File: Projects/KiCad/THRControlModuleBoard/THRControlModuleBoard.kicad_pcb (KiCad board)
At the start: 2 copper layers, 153.6 x 96.2 mm, 36 parts, among them IC1 LTC1480CN8#PBF, IC2 LTC1480CN8#PBF, J1 Conn_01x02_Socket, J2 Conn_01x02_Socket, J3 Screw_Terminal_01x02, J4 Conn_01x04_Socket, J5 Conn_01x04_Socket, J6 PCC-SMP-K-5, Q1 Q_PMOS_GDS, Q2 Q_PMOS_GDS, Q3 Q_PMOS_GDS, U1 LTC4416EMS#PBF, U2 MAX31856MUD+T, U3 NUCLEO-F303K8

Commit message: THRControlModuleを更新
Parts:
- moved IC1 45.0 mm to (181.8, 107.4)
- moved J4 45.0 mm to (182.1, 118.2)
- moved J3 42.3 mm to (180.5, 76.3)
- moved D1 37.1 mm to (168.7, 98.3)
- moved D2 37.1 mm to (165.6, 98.3)
- moved D3 37.1 mm to (171.7, 98.3)
- moved R7 37.1 mm to (165.6, 91.4)
- moved R8 37.1 mm to (171.7, 91.4)
- moved C3 37.1 mm to (152.9, 94.2)
- moved C4 37.1 mm to (152.9, 97.8)
- moved C6 37.1 mm to (152.9, 90.6)
- moved J6 37.1 mm to (159.1, 72.5)
- moved R6 37.1 mm to (168.7, 91.4)
- moved U2 37.1 mm to (158.5, 93.4)
- moved C5 37.1 mm to (158.8, 87.3)
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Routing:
- net RS485__ENABLE: track 0.00 -> 5.08 mm
- added copper zone on F.Cu, net Main Power Supply
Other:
- board size 153.6 x 96.2 mm -> 88.4 x 65.6 mm

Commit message: さーぼうごかしたい
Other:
- board size 88.4 x 65.6 mm -> 110 x 95.2 mm
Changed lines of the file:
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@@
   )
   (setup
+    (stackup
+      (layer "F.SilkS" (type "Top Silk Screen"))
+      (layer "F.Paste" (type "Top Solder Paste"))
+      (layer "F.Mask" (type "Top Solder Mask") (thickness 0.01))
+      (layer "F.Cu" (type "copper") (thickness 0.035))
+      (layer "dielectric 1" (type "core") (thickness 1.51) (material "FR4") (epsilon_r 4.5) (loss_tangent 0.02))
+      (layer "B.Cu" (type "copper") (thickness 0.035))
+      (layer "B.Mask" (type "Bottom Solder Mask") (thickness 0.01))
+      (layer "B.Paste" (type "Bottom Solder Paste"))
+      (layer "B.SilkS" (type "Bottom Silk Screen"))
+      (copper_finish "None")
+      (dielectric_constraints no)
+    )
     (pad_to_mask_clearance 0)
     (pcbplotparams
@@
     )
   )
-  (gr_line (start 187.7 126) (end 109.9 126)
-    (stroke (width 0.1) (type default)) (layer "Edge.Cuts"))
-  (gr_line (start 191.01 60.431) (end 102.61 60.431)
-    (stroke (width 0.1) (type default)) (layer "Edge.Cuts"))
+  (gr_circle (center 145.4 96.6) (end 145.5 96.6)
+    (stroke (width 0.0001) (type solid)) (fill solid) (layer "Edge.Cuts"))
+  (gr_circle (center 145.4 96.6) (end 145.5 96.6)
+    (stroke (width 0.0001) (type solid)) (fill solid) (layer "Edge.Cuts"))
+  (gr_arc (start 107.890168 136.6) (mid 145.4 41.375474) (end 182.909832 136.6)
+    (stroke (width 0.2) (type solid)) (layer "Edge.Cuts"))
+  (gr_circle (center 145.4 96.6) (end 145.5 96.6)
+    (stroke (width 0.0001) (type solid)) (fill solid) (layer "Edge.Cuts"))
+  (gr_circle (center 145.4 96.6) (end 145.5 96.6)
+    (stroke (width 0.0001) (type solid)) (fill solid) (layer "Edge.Cuts"))
+  (gr_circle (center 145.4 96.6) (end 145.5 96.6)
+    (stroke (width 0.0001) (type solid)) (fill solid) (layer "Edge.Cuts"))
+  (gr_circle (center 145.4 96.6) (end 145.5 96.6)
+    (stroke (width 0.0001) (type solid)) (fill solid) (layer "Edge.Cuts"))
+  (gr_circle (center 145.4 96.6) (end 145.5 96.6)
+    (stroke (width 0.0001) (type solid)) (fill solid) (layer "Edge.Cuts"))
+  (gr_circle (center 145.4 96.6) (end 145.5 96.6)
+    (stroke (width 0.0001) (type solid)) (fill solid) (layer "Edge.Cuts"))
+  (gr_circle (center 145.4 96.6) (end 145.5 96.6)
+    (stroke (width 0.0001) (type solid)) (fill solid) (layer "Edge.Cuts"))
+  (gr_circle (center 145.4 96.6) (end 145.5 96.6)
+    (stroke (width 0.0001) (type solid)) (fill solid) (layer "Edge.Cuts"))
+  (gr_circle (center 145.4 96.6) (end 145.5 96.6)
+    (stroke (width 0.0001) (type solid)) (fill solid) (layer "Edge.Cuts"))
+  (gr_circle (center 145.4 96.6) (end 145.5 96.6)
+    (stroke (width 0.0001) (type solid)) (fill solid) (layer "Edge.Cuts"))
+  (gr_line (start 182.909832 136.6) (end 107.890168 136.6)
+    (stroke (width 0.2) (type solid)) (layer "Edge.Cuts"))
+  (gr_circle (center 145.4 96.6) (end 145.5 96.6)
+    (stroke (width 0.0001) (type solid)) (fill solid) (layer "Edge.Cuts"))
+  (gr_circle (center 145.4 96.6) (end 145.5 96.6)
+    (stroke (width 0.0001) (type solid)) (fill solid) (layer "Edge.Cuts"))
+  (gr_circle (center 145.4 96.6) (end 145.5 96.6)
+    (stroke (width 0.0001) (type solid)) (fill solid) (layer "Edge.Cuts"))
   (segment (start 114.51 68.7485) (end 114.51 70.7535) (width 1) (layer "F.Cu") (net 1))
   (segment (start 123.912 77.184) (end 123.912 80.4215) (width 0.25) (layer "F.Cu") (net 1))
@@
     )
   )
+  (group "" (id 6e8ac5b0-bd87-4622-b2de-0a6718457d24)
+    (members
+      02eda940-add0-4b54-9729-b477d0ac1bd8
+      0f6cd9d3-a6ce-4f51-8e13-86931dcd8bd2
+      16407f10-dc8b-4954-87af-a99fab043be2
+      1663ffb2-55dc-4813-a6c3-30438c59a478
+      2d43c464-5b90-429b-b19e-6585a19991ff
+      2ef0aaf6-961e-416b-b369-ce24fa3bbbf0
+      54b76117-5f5b-4763-8b0f-193e03239677
+      6ae3d9e0-deb5-44b5-9874-15ed370a52bc
+      7051c1c9-aa6a-4af1-a04f-d4374640d7f7
+      7994f68a-6575-4db6-a7d5-2af3b2de868c
+      9ebd4081-3d82-469b-948d-cb647f83ce62
+      adc2bde1-7d6a-4060-a991-f76b2fa04667
+      da316a41-3531-4383-ad27-9925a38623bb
+      de768a8c-8413-48a7-8f38-190f8ccf8624
+      dec51251-748c-4501-a1a5-cca1334c7dda
+      dfc7496d-4f87-4a89-9541-c43c7443b227
+      e50dee0a-0c97-447f-b977-912c927439fb
+    )
+  )

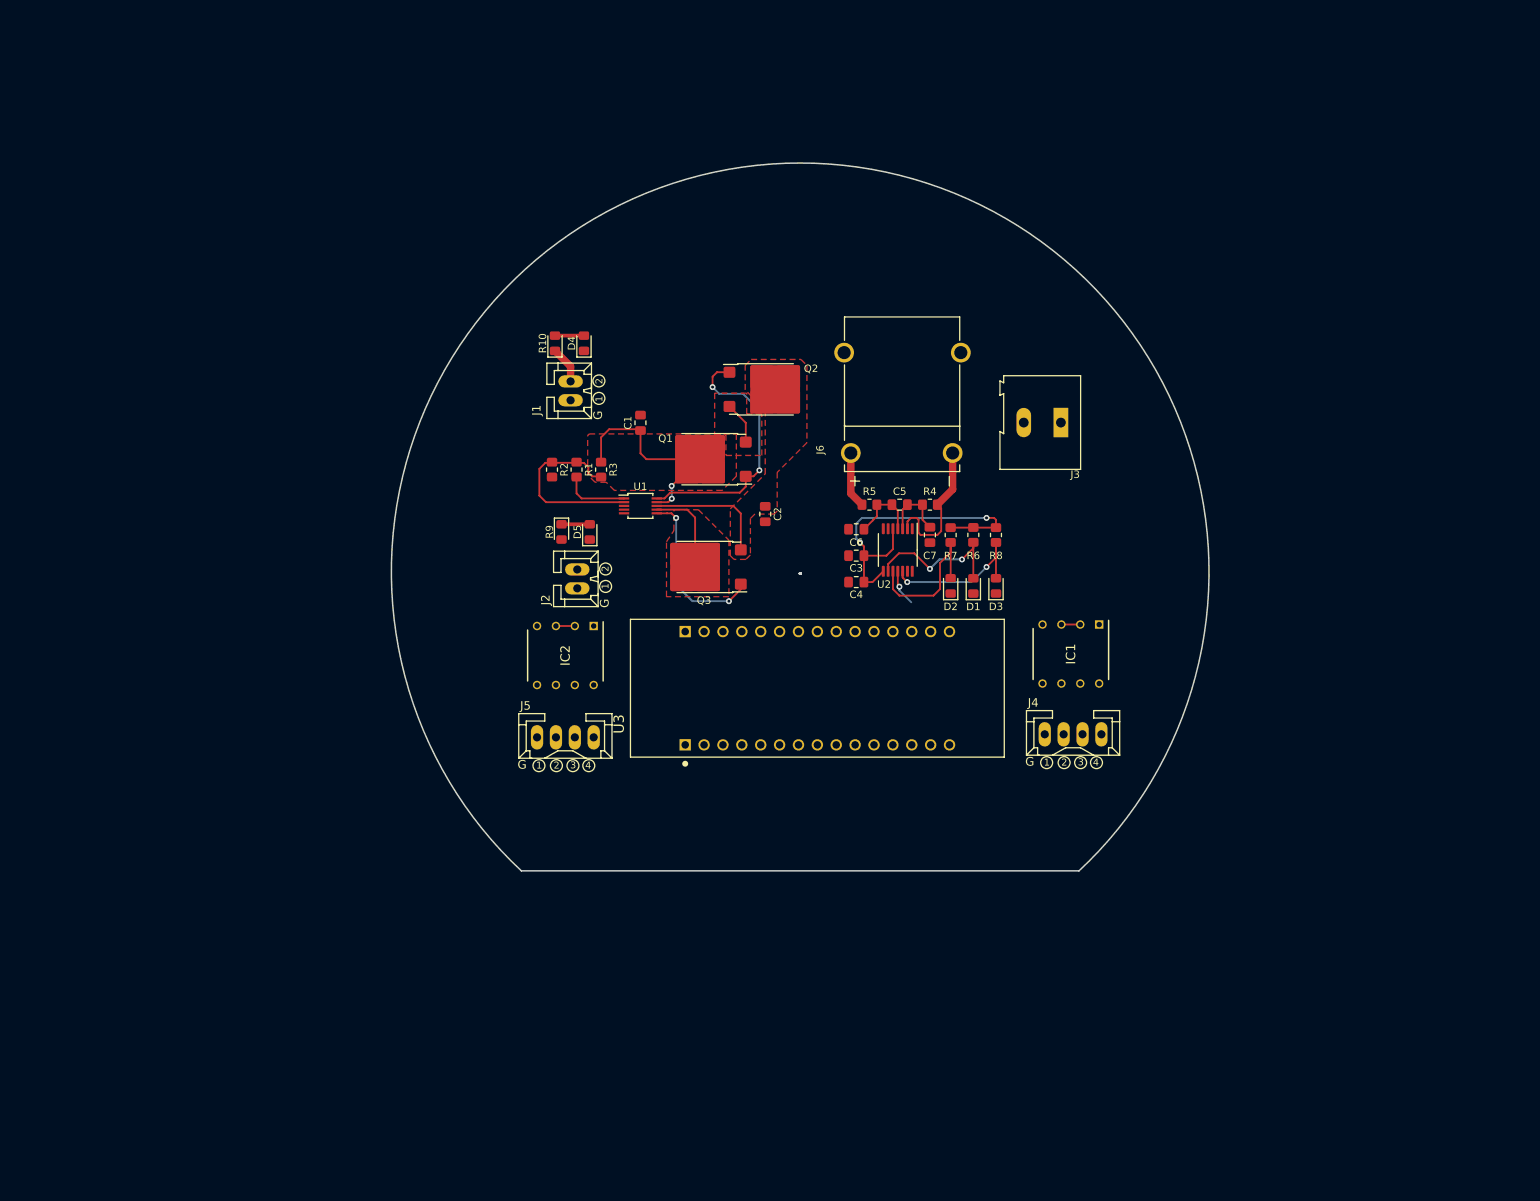
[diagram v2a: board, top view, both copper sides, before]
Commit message: 取付穴位置等を追加
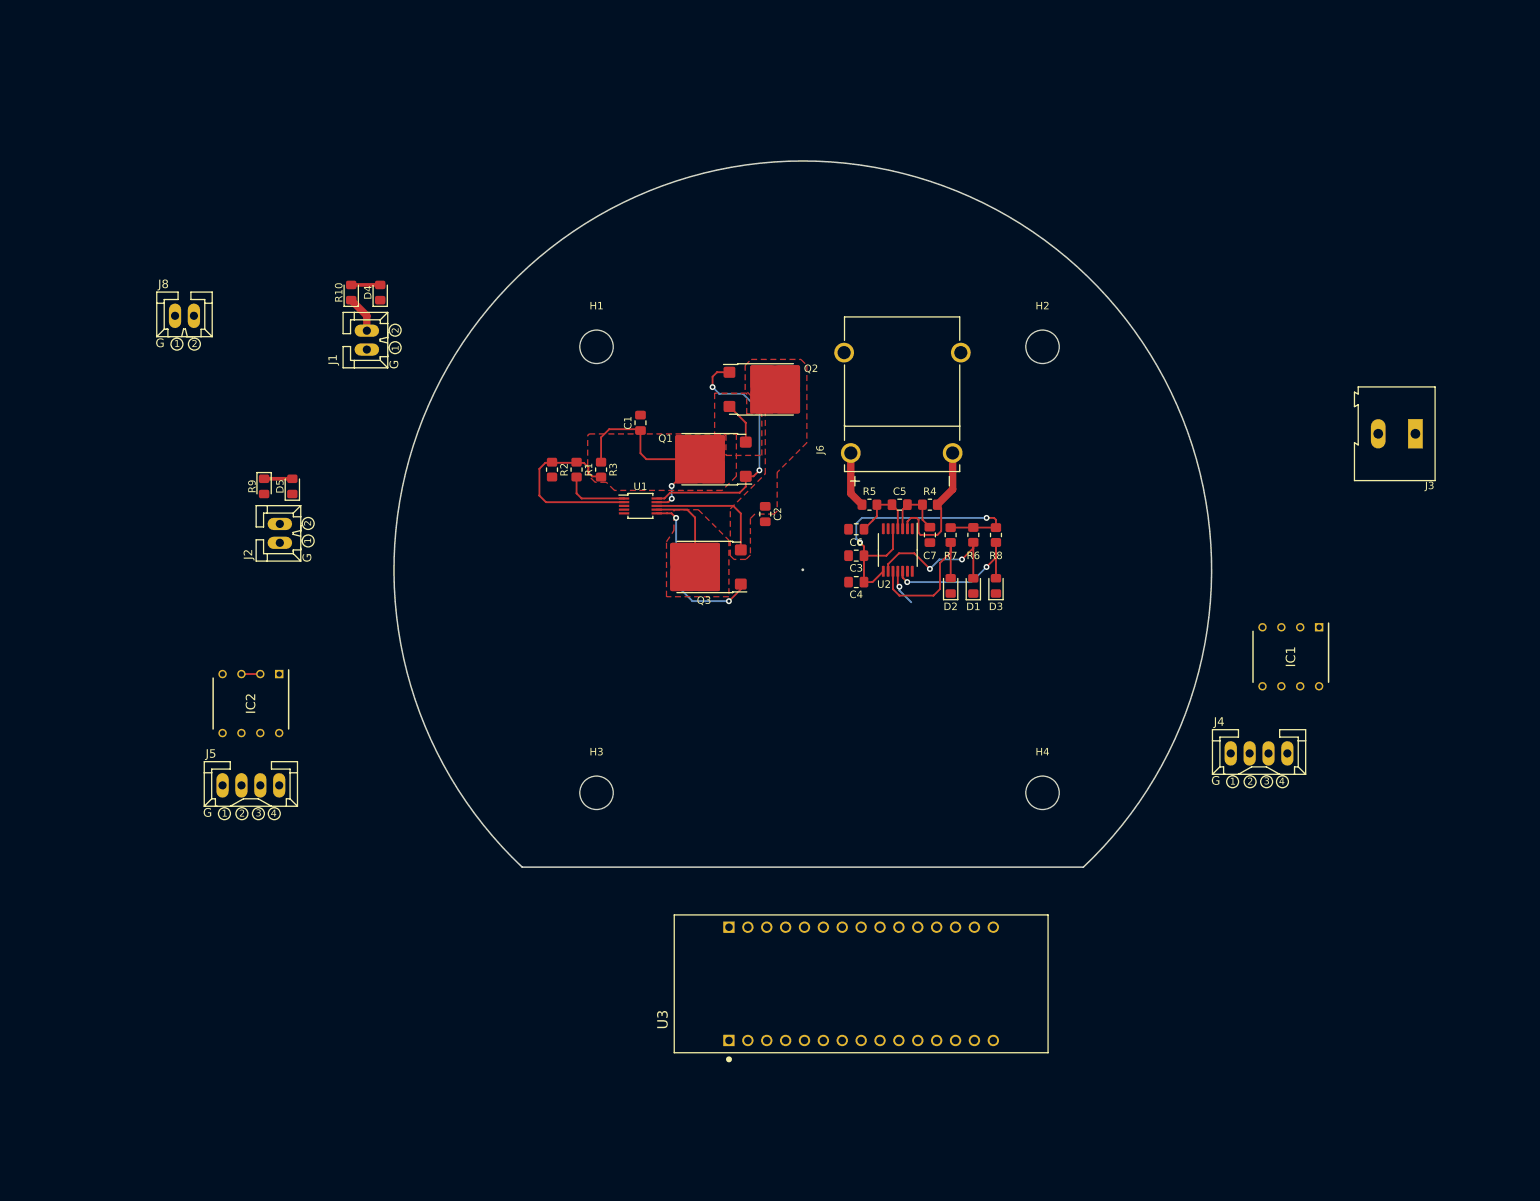
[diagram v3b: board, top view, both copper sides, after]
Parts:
- added H1: MountingHole, MountingHole:MountingHole_4.5mm, F.Cu at (118.0, 66.1)
- added H2: MountingHole, MountingHole:MountingHole_4.5mm, F.Cu at (178.0, 66.1)
- added H3: MountingHole, MountingHole:MountingHole_4.5mm, F.Cu at (118.0, 126.1)
- added H4: MountingHole, MountingHole:MountingHole_4.5mm, F.Cu at (178.0, 126.1)
- added J8: Conn_01x02_Socket, CONNECTOR:CONNECTOR_2-STRAIGHT, F.Cu at (62.6, 61.9)
- moved J3 47.7 mm to (228.2, 77.8)
- moved IC2 42.8 mm to (71.5, 114.1)
- moved J5 42.8 mm to (71.5, 125.1)
- moved D5 40.5 mm to (77.1, 84.9)
- moved R9 40.5 mm to (73.3, 84.9)
- moved J2 40.5 mm to (75.4, 91.2)
- moved U3 40.2 mm to (153.6, 151.8)
- moved IC1 29.6 mm to (211.4, 107.8)
- moved J1 28.2 mm to (87.1, 65.2)
- moved D4 28.2 mm to (88.9, 58.8)
- moved R10 28.2 mm to (85.0, 58.8)
- moved J4 25.2 mm to (207.1, 120.8)
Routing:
- net RS485__ENABLE: track 5.08 -> 2.54 mm
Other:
- board size 110 x 95.2 mm -> 110 x 95 mm

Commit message: コミットのためにステージ変更
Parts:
- moved IC1 10.5 mm to (213.7, 97.6)
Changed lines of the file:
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@@
   )
   (footprint "LTC1480CN8#PBF:DIP794W53P254L1016H394Q8N" (layer "F.Cu")
-    (at 211.4 107.8 -90)
+    (at 213.7 97.6 -90)
     (descr "N8 Package 8-Lead PDIP")
     (tags "Integrated Circuit")

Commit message: KiCADを更新
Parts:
- removed U3: NUCLEO-F303K8, NUCLEO-F303K8:MODULE_NUCLEO-F303K8
- added A1: Arduino_Nano_Every, Module:Arduino_Nano, F.Cu at (198.0, 27.6)
- added C8: 0.1, Capacitor_SMD:C_0805_2012Metric_Pad1.18x1.45mm_HandSolder, F.Cu at (231.3, 37.0)
- added C9: 0.1, Capacitor_SMD:C_0805_2012Metric_Pad1.18x1.45mm_HandSolder, F.Cu at (231.4, 42.2)
- added IC1: LTC1480CN8#PBF, LTC1480CN8#PBF:DIP794W53P254L1016H394Q8N, F.Cu at (220.7, 28.8)
- added IC2: LTC1480CN8#PBF, LTC1480CN8#PBF:DIP794W53P254L1016H394Q8N, F.Cu at (231.6, 28.8)
- added J4: Conn_01x04_Socket, CONNECTOR:CONNECTOR_4-STRAIGHT, F.Cu at (221.8, 40.5)
- added J5: Conn_01x04_Socket, CONNECTOR:CONNECTOR_4-STRAIGHT, F.Cu at (222.1, 53.0)
- added JP1: SolderJumper_2_Bridged, Jumper:SolderJumper-2_P1.3mm_Open_TrianglePad1.0x1.5mm, F.Cu at (241.3, 24.8)
- added JP2: SolderJumper_2_Bridged, Jumper:SolderJumper-2_P1.3mm_Open_TrianglePad1.0x1.5mm, F.Cu at (241.3, 28.3)
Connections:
- C3 pad 1: +3.3V -> NanoEvery_3.3V
- C4 pad 1: +3.3V -> NanoEvery_3.3V
- D1 pad 1: /STM32F303K8/SPI__~{CS}-~{CS} -> /NanoEvery/MAX31856__~{CS}-~{CS}
- D2 pad 1: /STM32F303K8/SPI__SCK-SCLK -> /NanoEvery/MAX31856__SCK-SCLK
- D3 pad 1: /STM32F303K8/SPI__SDI-MOSI -> /NanoEvery/MAX31856__SDI-MOSI
- R6 pad 1: +3.3V -> NanoEvery_3.3V
- R7 pad 1: +3.3V -> NanoEvery_3.3V
- R8 pad 1: +3.3V -> NanoEvery_3.3V
- U2 pad 11: /STM32F303K8/SPI__SDO-MISO -> /NanoEvery/MAX31856__SDO-MISO
- U2 pad 5: +3.3V -> NanoEvery_3.3V
- U2 pad 8: +3.3V -> NanoEvery_3.3V
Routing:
- net NanoEvery_3.3V: track 0.00 -> 44.9 mm, vias 0 -> 2
- net +3.3V: track 44.9 -> 0.00 mm, vias 2 -> 0
- net /STM32F303K8/SPI__SDO-MISO: track 4.92 -> 0.00 mm, vias 1 -> 0
- net /NanoEvery/MAX31856__SDO-MISO: track 0.00 -> 4.92 mm, vias 0 -> 1

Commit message: KiCADを更新
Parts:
- added JP3: SolderJumper_2_Bridged, Jumper:SolderJumper-2_P1.3mm_Open_TrianglePad1.0x1.5mm, F.Cu at (180.5, 28.6)
- added JP4: SolderJumper_2_Bridged, Jumper:SolderJumper-2_P1.3mm_Open_TrianglePad1.0x1.5mm, F.Cu at (180.5, 32.1)
- added JP5: SolderJumper_2_Bridged, Jumper:SolderJumper-2_P1.3mm_Open_TrianglePad1.0x1.5mm, F.Cu at (180.5, 35.6)
- added JP6: SolderJumper_2_Bridged, Jumper:SolderJumper-2_P1.3mm_Open_TrianglePad1.0x1.5mm, F.Cu at (180.5, 39.2)
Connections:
- A1 pad 12: unconnected-(A1-D9-Pad12) -> /NanoEvery/MAX31856__DRDY-DRDY
- A1 pad 13: unconnected-(A1-D10-Pad13) -> /NanoEvery/MAX31856__FAULT-FAULT
- A1 pad 14: /NanoEvery/MAX31856__SDI-MOSI -> /NanoEvery/SPI__SDI-MOSI
- A1 pad 15: /NanoEvery/MAX31856__SDO-MISO -> /NanoEvery/SPI__SDO-MISO
- A1 pad 16: /NanoEvery/MAX31856__SCK-SCLK -> /NanoEvery/SPI__SCK-SCLK
- A1 pad 7: /NanoEvery/MAX31856__DRDY-DRDY -> MAX31855__~{CS}-~{CS}
- A1 pad 8: /NanoEvery/MAX31856__FAULT-FAULT -> unconnected-(A1-D5-Pad8)
- D1 pad 1: /NanoEvery/MAX31856__~{CS}-~{CS} -> Net-(D1-K)
- D2 pad 1: /NanoEvery/MAX31856__SCK-SCLK -> Net-(D2-K)
- D3 pad 1: /NanoEvery/MAX31856__SDI-MOSI -> Net-(D3-K)
- U2 pad 11: /NanoEvery/MAX31856__SDO-MISO -> Net-(JP3-A)
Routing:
- net Net-(JP3-A): track 0.00 -> 4.92 mm, vias 0 -> 1
- net /NanoEvery/MAX31856__SDO-MISO: track 4.92 -> 0.00 mm, vias 1 -> 0
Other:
- board outline removed
